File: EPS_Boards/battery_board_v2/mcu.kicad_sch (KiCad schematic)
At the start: 14 parts

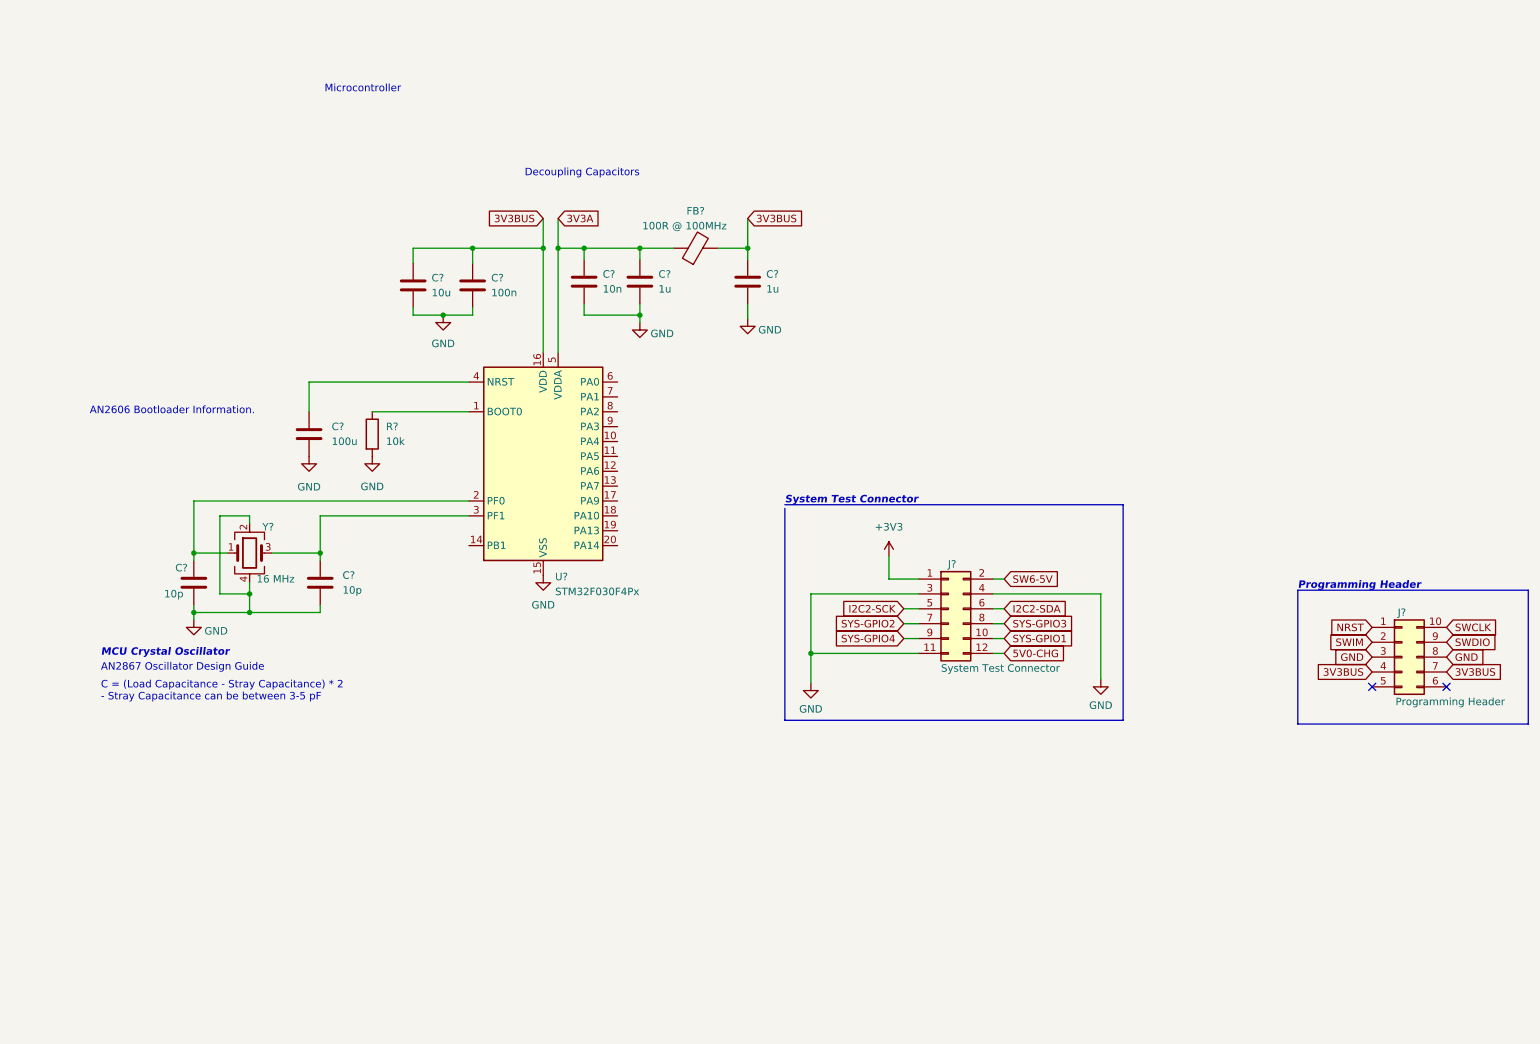
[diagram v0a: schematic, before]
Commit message: eps: battery board: updated schematic
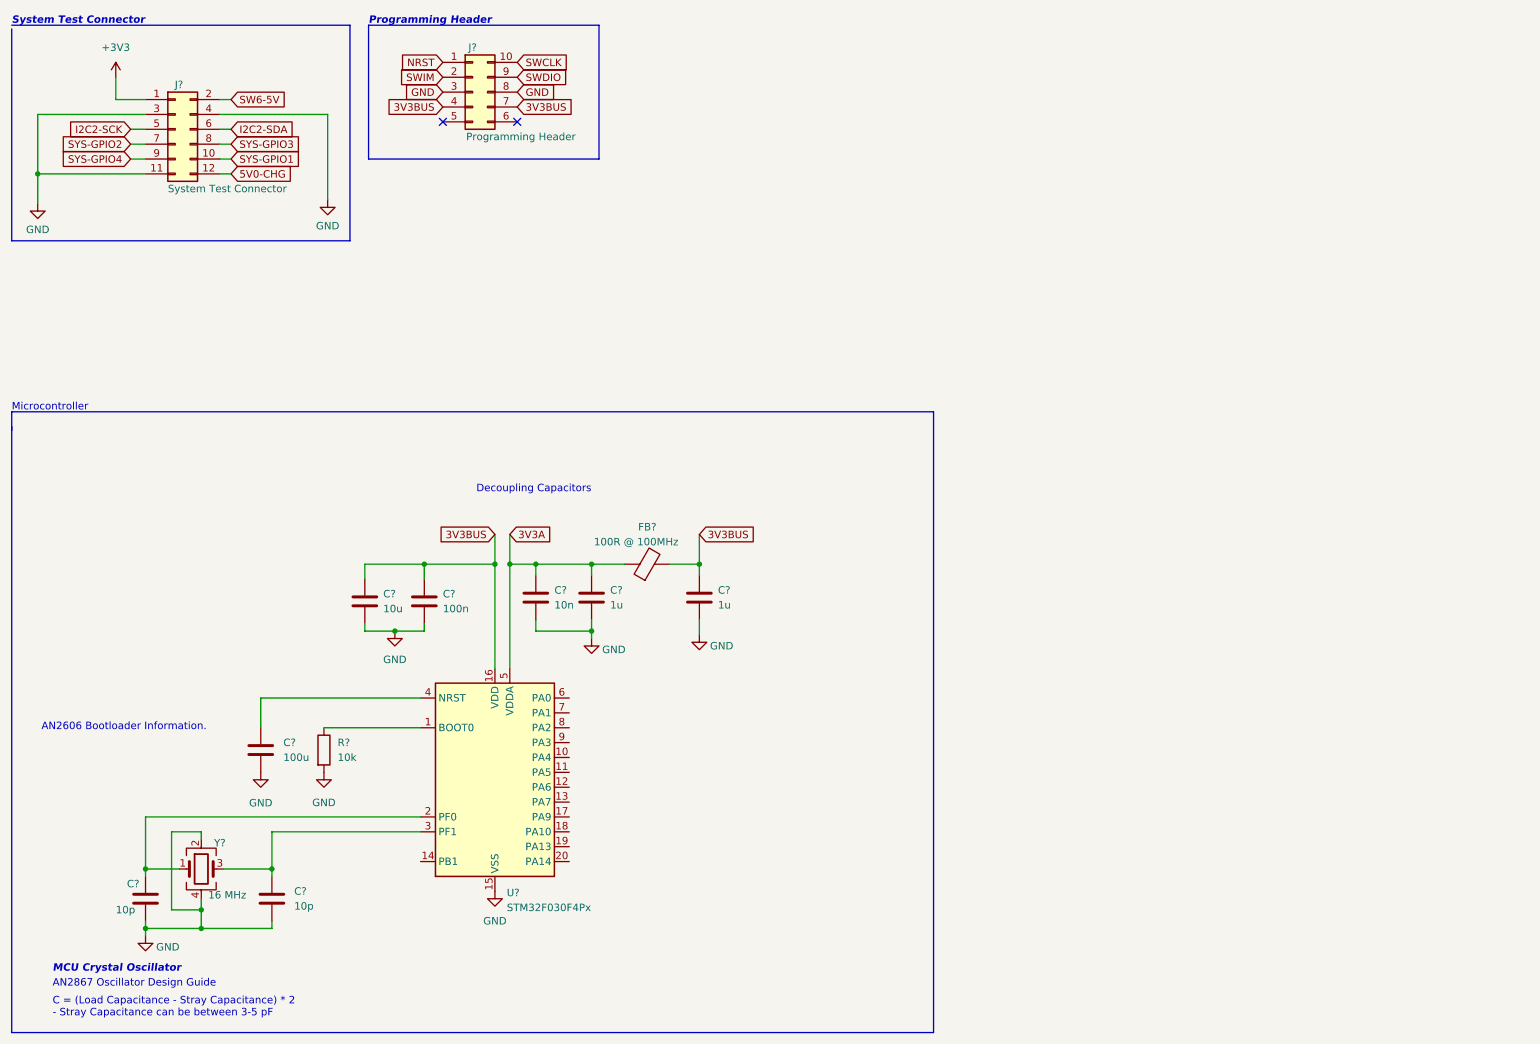
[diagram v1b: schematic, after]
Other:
- moved on the sheet: C?, FB?, J?, R?, U?, Y?

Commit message: eps: battery board: updated board layout
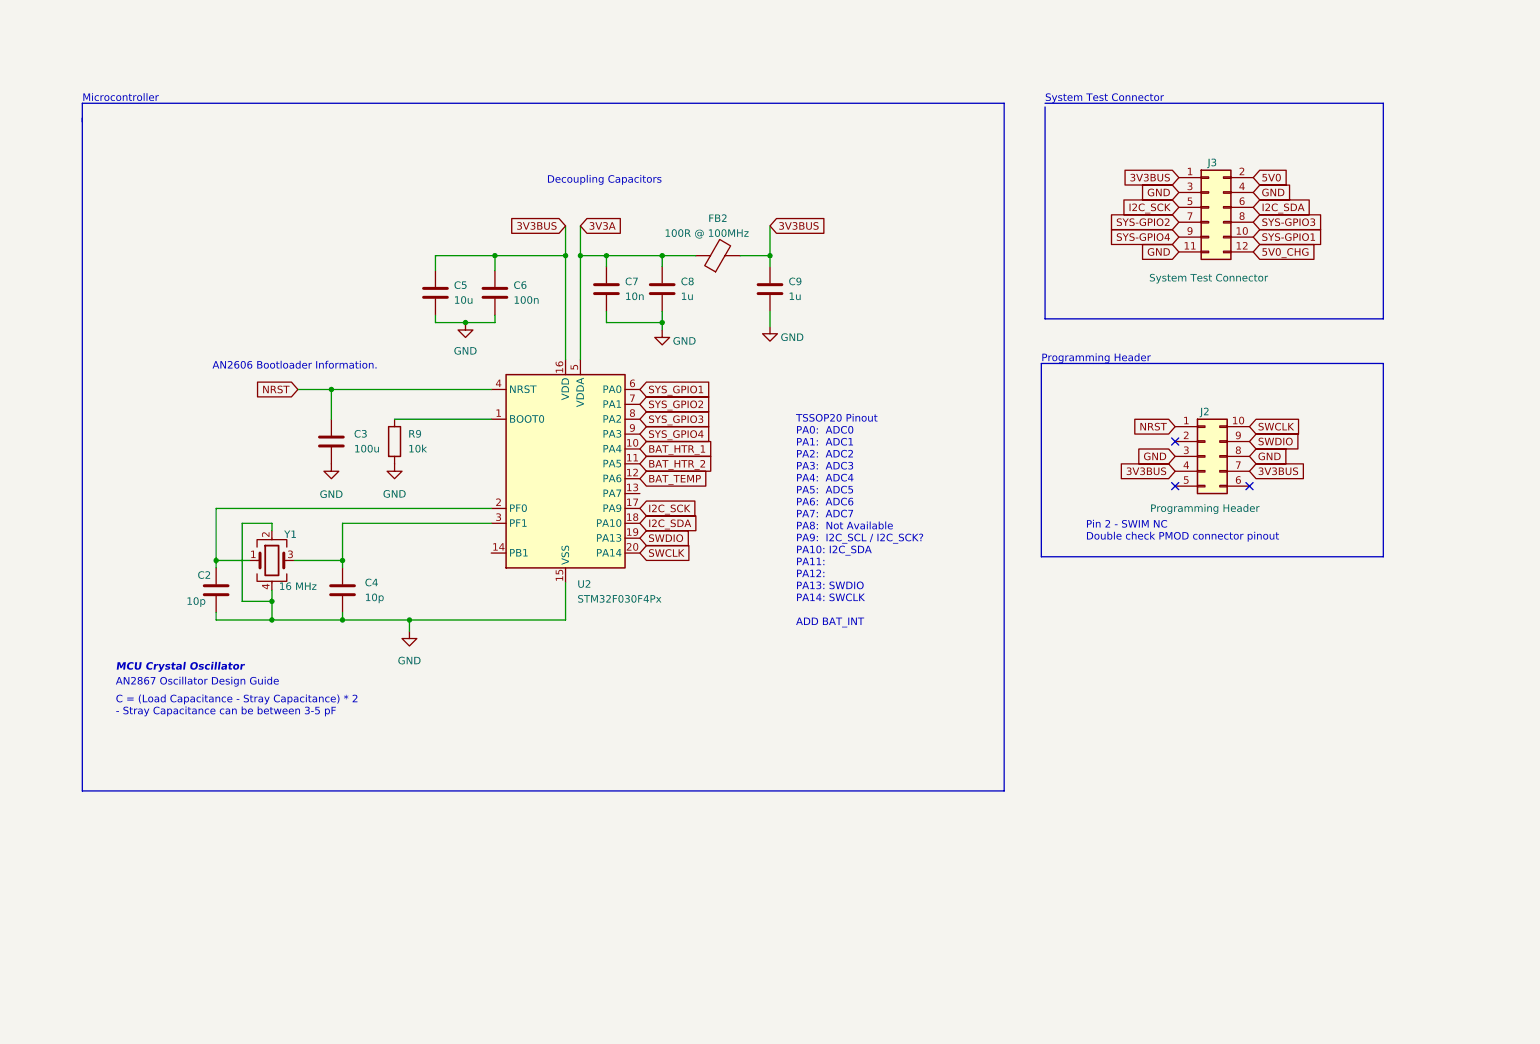
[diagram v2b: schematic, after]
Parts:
- C2, C4, C5, C6, C7, C8, C9: renamed from C?; footprint Capacitor_SMD:C_0603_1608Metric -> Capacitor_SMD:C_0402_1005Metric
- C3: renamed from C?; footprint (none) -> Capacitor_SMD:C_0402_1005Metric
- J2: renamed from J?; footprint Connector_PinSocket_2.54mm:PinSocket_2x05_P2.54mm_Horizontal -> Connector_PinSocket_2.54mm:PinSocket_2x05_P2.54mm_Vertical
- J3: renamed from J?; footprint Connector_PinSocket_2.54mm:PinSocket_2x06_P2.54mm_Horizontal -> Connector_PinSocket_2.54mm:PinSocket_2x06_P2.54mm_Vertical
- R9: renamed from R?; footprint (none) -> Resistor_SMD:R_0402_1005Metric
- gave numbers to parts that had none: 3
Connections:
- net +3V3 is gone; now on net 3V3BUS: J3.1 (Pin_1)
- net I2C2-SCK is gone; now on net I2C_SCK: J3.5 (Pin_5)
- net I2C2-SDA is gone; now on net I2C_SDA: J3.6 (Pin_6)
- net NRST: now also C3.1, U2.4 (NRST)
- net SWCLK: now also U2.20 (PA14)
- net SWDIO: now also U2.19 (PA13)
- net BAT_HTR_1: now reaches U2.10 (PA4)
- net BAT_HTR_2: now reaches U2.11 (PA5)
- net BAT_TEMP: now reaches U2.12 (PA6)
- net I2C_SCK: now reaches U2.17 (PA9)
- net I2C_SDA: now reaches U2.18 (PA10)
- net SYS_GPIO1: now reaches U2.6 (PA0)
- net SYS_GPIO2: now reaches U2.7 (PA1)
- net SYS_GPIO3: now reaches U2.8 (PA2)
- net SYS_GPIO4: now reaches U2.9 (PA3)
- net 5V0-CHG renamed 5V0_CHG
- net SW6-5V renamed 5V0
- net SWIM: no longer names the net of J2.2 (Pin_2)
- no-connect marks 2 -> 3
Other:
- note added: "Pin 2 - SWIM NC Double check PMOD connector pinout"
- note added: "TSSOP20 Pinout PA0: ADC0 PA1: ADC1 PA2: ADC2 PA3: ADC3 PA4: ADC4 PA5: ADC5 PA6: ADC6 PA7: ADC7 PA8: Not Available PA9: I2C_SCL / I2C_SCK? PA10: I2C_SDA PA11: PA12: PA13: SWDIO PA14: SWCLK ADD BAT_INT"
- moved on the sheet: C2, C3, C4, C5, C6, C7, C8, C9, FB2, J2, J3, R9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

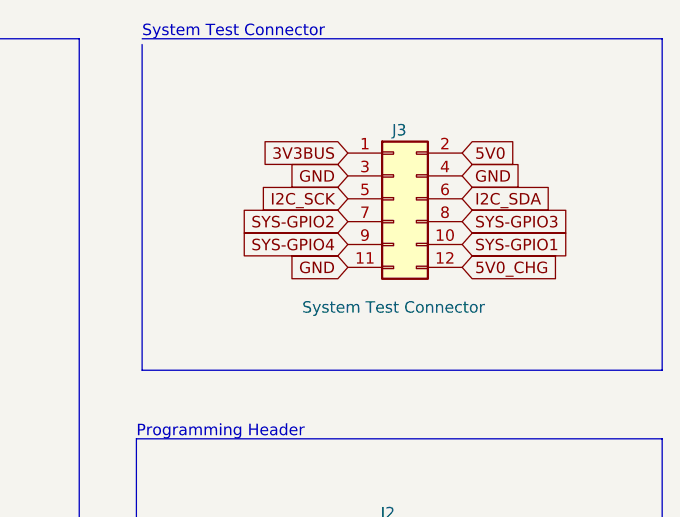
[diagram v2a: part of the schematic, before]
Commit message: eps: battery board: more updates to layout
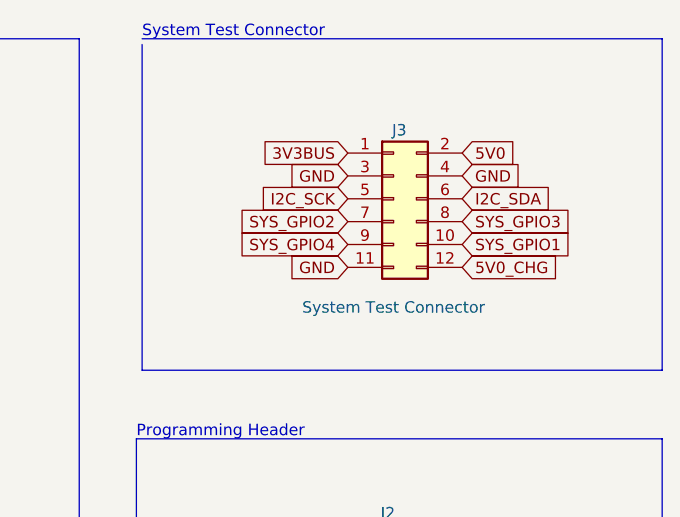
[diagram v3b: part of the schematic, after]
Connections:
- net SYS-GPIO1 is gone; now on net SYS_GPIO1: J3.10 (Pin_10)
- net SYS-GPIO2 is gone; now on net SYS_GPIO2: J3.7 (Pin_7)
- net SYS-GPIO3 is gone; now on net SYS_GPIO3: J3.8 (Pin_8)
- net SYS-GPIO4 is gone; now on net SYS_GPIO4: J3.9 (Pin_9)
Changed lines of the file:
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@@
     )
   )
-  (global_label "SYS-GPIO4" (shape input) (at 216.535 55.88 180) (fields_autoplaced)
+  (global_label "SYS_GPIO4" (shape input) (at 216.535 55.88 180) (fields_autoplaced)
     (effects (font (size 1.27 1.27)) (justify right))
-    (property "Intersheet References" "${INTERSHEET_REFS}" (id 0) (at 203.3571 55.8006 0)
+    (property "Intersheet References" "${INTERSHEET_REFS}" (id 0) (at 204.0508 55.8006 0)
       (effects (font (size 1.27 1.27)) (justify right) hide)
     )
@@
     )
   )
-  (global_label "SYS-GPIO2" (shape input) (at 216.535 53.34 180) (fields_autoplaced)
+  (global_label "SYS_GPIO2" (shape input) (at 216.535 53.34 180) (fields_autoplaced)
     (effects (font (size 1.27 1.27)) (justify right))
-    (property "Intersheet References" "${INTERSHEET_REFS}" (id 0) (at 203.3571 53.2606 0)
+    (property "Intersheet References" "${INTERSHEET_REFS}" (id 0) (at 204.0508 53.2606 0)
       (effects (font (size 1.27 1.27)) (justify right) hide)
     )
@@
     )
   )
-  (global_label "SYS-GPIO1" (shape input) (at 229.235 55.88 0) (fields_autoplaced)
+  (global_label "SYS_GPIO1" (shape input) (at 229.235 55.88 0) (fields_autoplaced)
     (effects (font (size 1.27 1.27)) (justify left))
-    (property "Intersheet References" "${INTERSHEET_REFS}" (id 0) (at 242.324 55.8006 0)
+    (property "Intersheet References" "${INTERSHEET_REFS}" (id 0) (at 241.7192 55.8006 0)
       (effects (font (size 1.27 1.27)) (justify left) hide)
     )
@@
     )
   )
-  (global_label "SYS-GPIO3" (shape input) (at 229.235 53.34 0) (fields_autoplaced)
+  (global_label "SYS_GPIO3" (shape input) (at 229.235 53.34 0) (fields_autoplaced)
     (effects (font (size 1.27 1.27)) (justify left))
-    (property "Intersheet References" "${INTERSHEET_REFS}" (id 0) (at 242.4129 53.2606 0)
+    (property "Intersheet References" "${INTERSHEET_REFS}" (id 0) (at 241.7192 53.2606 0)
       (effects (font (size 1.27 1.27)) (justify left) hide)
     )

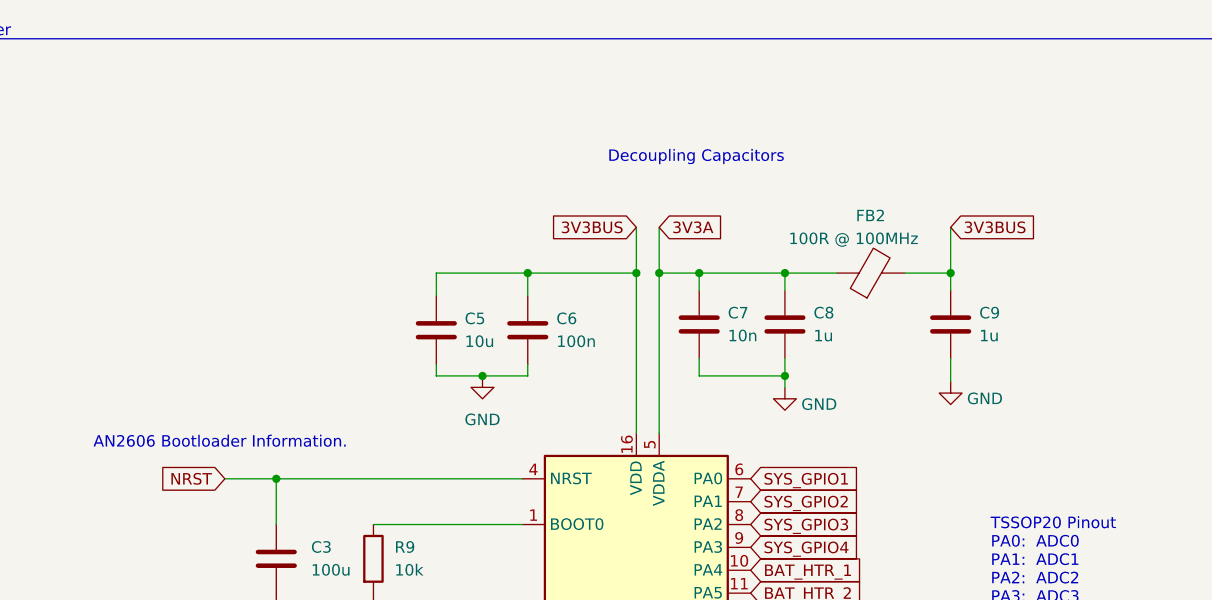
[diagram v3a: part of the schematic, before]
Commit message: eps: battery board: added EDS protection
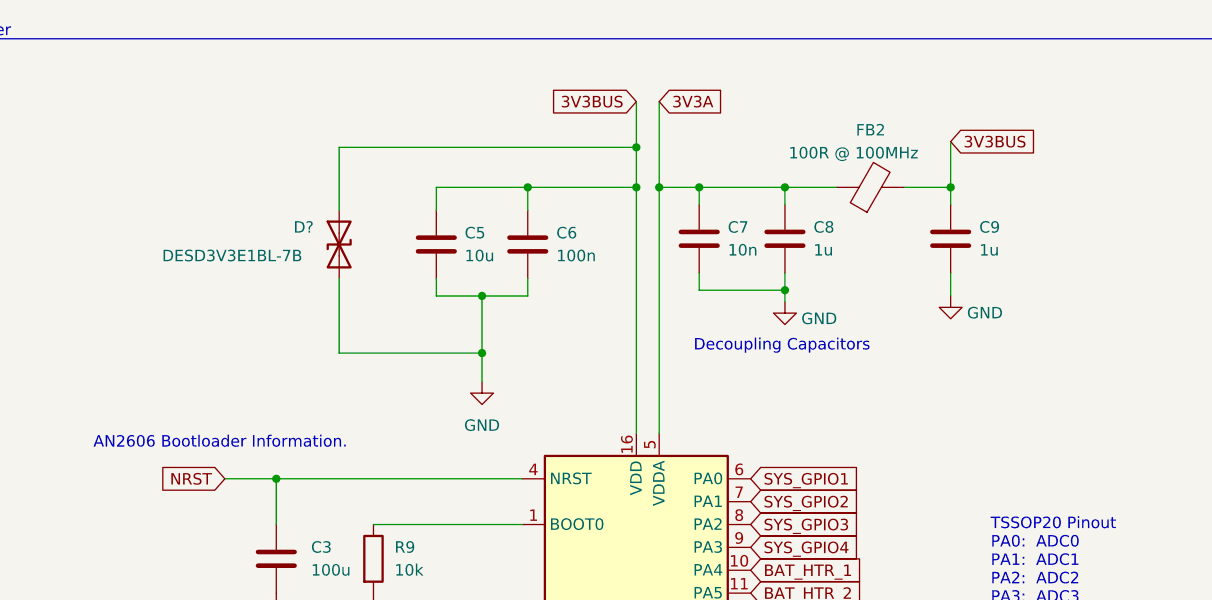
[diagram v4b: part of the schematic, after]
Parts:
- added D?: DESD3V3E1BL-7B, Resistor_SMD:R_0201_0603Metric, symbol Device:D_TVS
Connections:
- net 3V3BUS: now also D?.1 (A1)
- net GND: now also D?.2 (A2)
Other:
- moved on the sheet: C5, C6, C7, C8, C9, FB2

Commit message: eps: battery board: progress on pcb layout
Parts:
- gave numbers to parts that had none: 1
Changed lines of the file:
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@@
   (symbol (lib_id "Device:D_TVS") (at 78.74 55.88 90) (mirror x) (unit 1)
     (in_bom yes) (on_board yes)
-    (property "Reference" "D?" (id 0) (at 73.66 53.975 90)
+    (property "Reference" "D2" (id 0) (at 73.66 53.975 90)
       (effects (font (size 1.27 1.27)) (justify right))
     )
